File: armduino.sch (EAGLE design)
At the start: 64 parts, among them IC1 7805DT, IC2 LM358D, IC3 LM1117-3.3V, Q1 FDN360P, Q2 5MHz, Q3 8MHz, U1 MKL26Z128VFM4, U2 MKE02Z64VLD4, X1 POWERSUPPLY_DC21MMX, X2 USB-B_TH

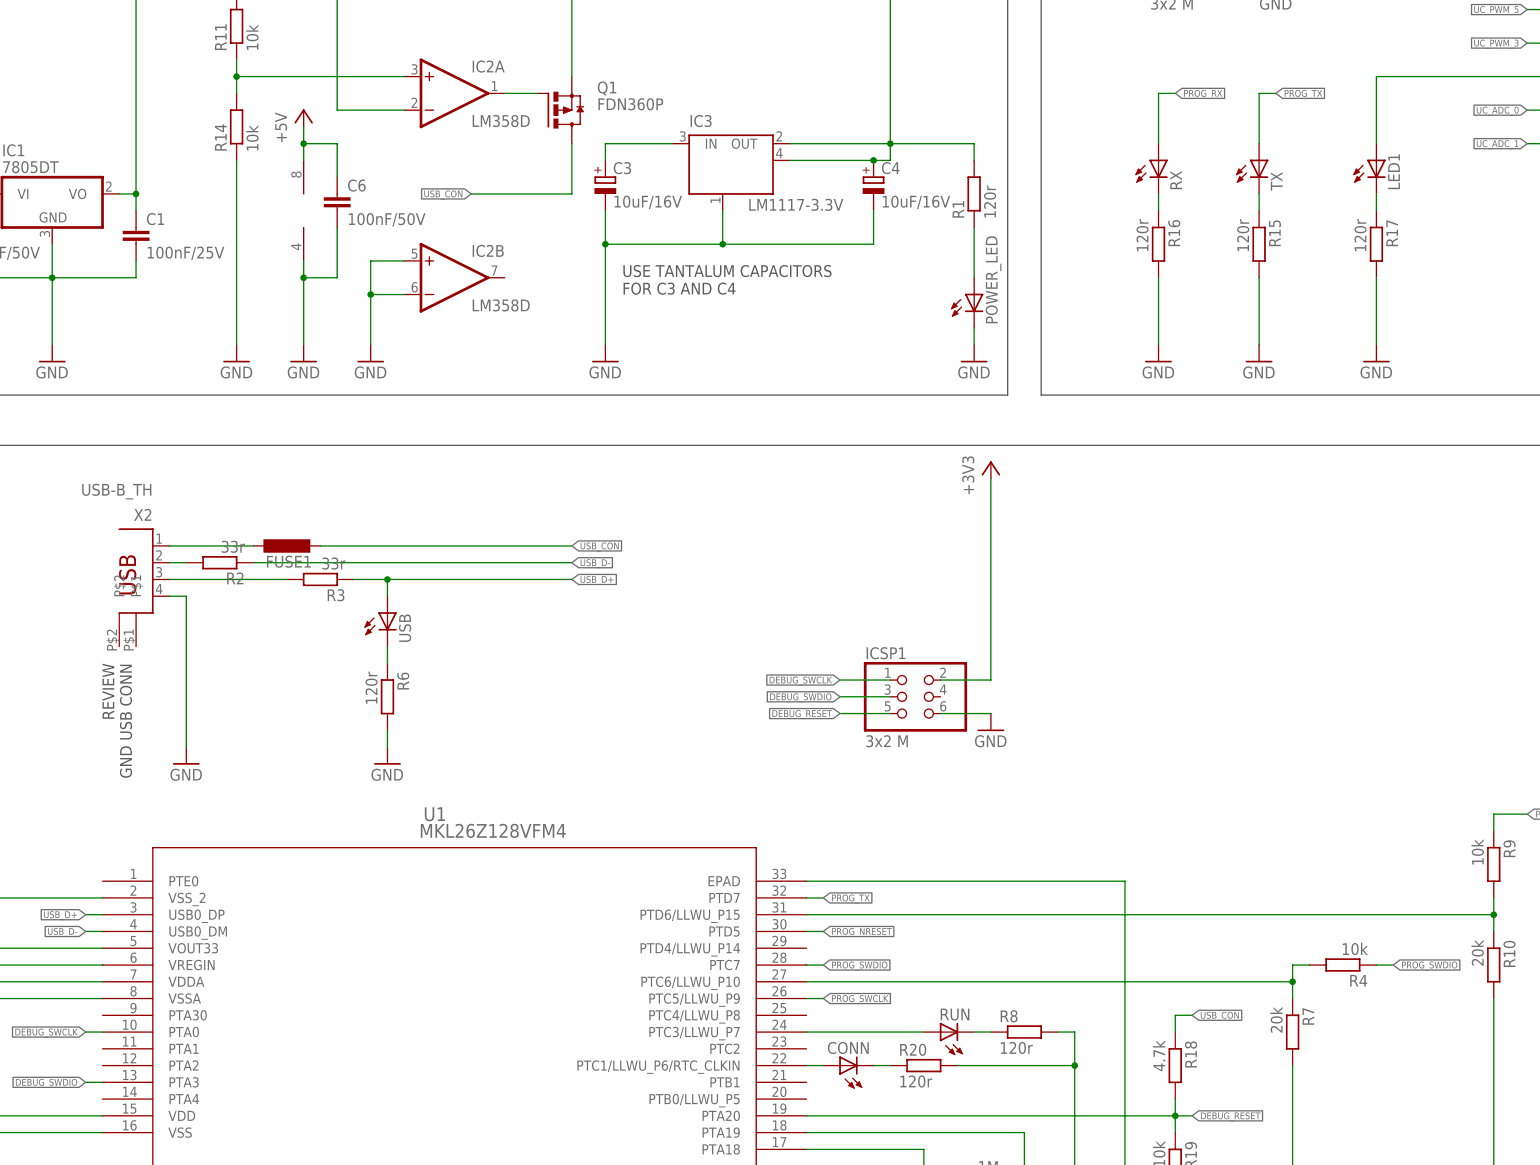
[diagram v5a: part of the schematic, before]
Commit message: Fixed target XTAL value, heat dissipation mask, update to version 0.7
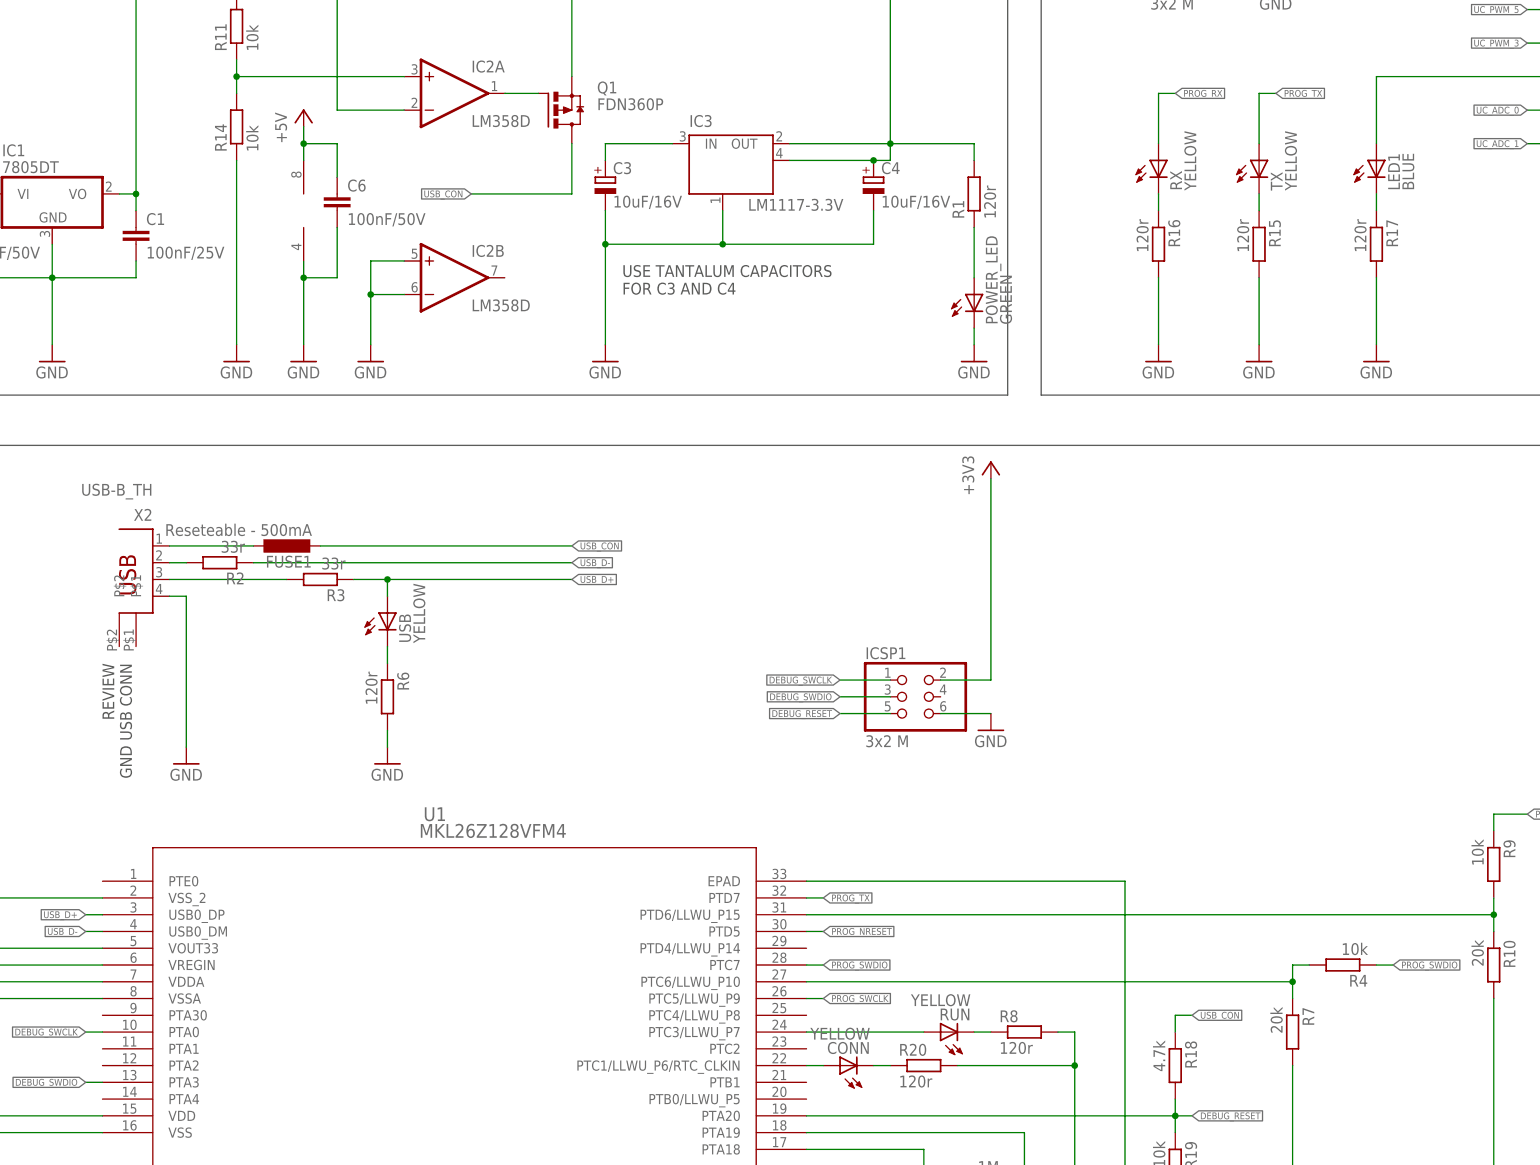
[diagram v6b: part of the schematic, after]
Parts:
- CONN, RUN, RX, TX, USB: value (none) -> YELLOW
- FUSE1: value (none) -> Reseteable - 500mA
- LED1: value (none) -> BLUE
- POWER_LED: value (none) -> GREEN
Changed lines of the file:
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@@
 <setting verticaltext="up"/>
 </settings>
-<grid distance="0.1" unitdist="inch" unit="inch" style="lines" multiple="1" display="yes" altdistance="0.01" altunitdist="inch" altunit="inch"/>
+<grid distance="0.1" unitdist="inch" unit="inch" style="lines" multiple="1" display="no" altdistance="0.01" altunitdist="inch" altunit="inch"/>
 <layers>
 <layer number="1" name="Top" color="4" fill="1" visible="no" active="no"/>
@@
 <part name="GND3" library="supply1" deviceset="GND" device=""/>
 <part name="D1" library="diode" deviceset="DIODE-" device="DO-214AC" value="1n4007"/>
-<part name="POWER_LED" library="led" deviceset="LED" device="CHIP-LED0805"/>
+<part name="POWER_LED" library="led" deviceset="LED" device="CHIP-LED0805" value="GREEN"/>
 <part name="R1" library="rcl" deviceset="R-EU_" device="M0805" value="120r"/>
 <part name="GND4" library="supply1" deviceset="GND" device=""/>
-<part name="FUSE1" library="rcl" deviceset="L-EU" device="L1812"/>
+<part name="FUSE1" library="rcl" deviceset="L-EU" device="L1812" value="Reseteable - 500mA"/>
 <part name="GND5" library="supply1" deviceset="GND" device=""/>
 <part name="R2" library="rcl" deviceset="R-EU_" device="M0805" value="33r"/>
 <part name="R3" library="rcl" deviceset="R-EU_" device="M0805" value="33r"/>
-<part name="USB" library="led" deviceset="LED" device="CHIP-LED0805"/>
+<part name="USB" library="led" deviceset="LED" device="CHIP-LED0805" value="YELLOW"/>
 <part name="R6" library="rcl" deviceset="R-EU_" device="M0805" value="120r"/>
 <part name="GND12" library="supply1" deviceset="GND" device=""/>
@@
 <part name="C17" library="rcl" deviceset="C-EU" device="C0805K" value="1uF/25V"/>
 <part name="GND22" library="supply1" deviceset="GND" device=""/>
-<part name="TX" library="led" deviceset="LED" device="CHIP-LED0805"/>
+<part name="TX" library="led" deviceset="LED" device="CHIP-LED0805" value="YELLOW"/>
 <part name="R15" library="rcl" deviceset="R-EU_" device="M0805" value="120r"/>
-<part name="RX" library="led" deviceset="LED" device="CHIP-LED0805"/>
+<part name="RX" library="led" deviceset="LED" device="CHIP-LED0805" value="YELLOW"/>
 <part name="R16" library="rcl" deviceset="R-EU_" device="M0805" value="120r"/>
 <part name="GND25" library="supply1" deviceset="GND" device=""/>
 <part name="GND26" library="supply1" deviceset="GND" device=""/>
 <part name="GND27" library="supply1" deviceset="GND" device=""/>
-<part name="LED1" library="led" deviceset="LED" device="CHIP-LED0805"/>
+<part name="LED1" library="led" deviceset="LED" device="CHIP-LED0805" value="BLUE"/>
 <part name="R17" library="rcl" deviceset="R-EU_" device="M0805" value="120r"/>
 <part name="GND28" library="supply1" deviceset="GND" device=""/>
@@
 <part name="R7" library="rcl" deviceset="R-EU_" device="M0805" value="20k"/>
 <part name="GND35" library="supply1" deviceset="GND" device=""/>
-<part name="RUN" library="led" deviceset="LED" device="CHIP-LED0805"/>
-<part name="CONN" library="led" deviceset="LED" device="CHIP-LED0805"/>
+<part name="RUN" library="led" deviceset="LED" device="CHIP-LED0805" value="YELLOW"/>
+<part name="CONN" library="led" deviceset="LED" device="CHIP-LED0805" value="YELLOW"/>
 <part name="R8" library="rcl" deviceset="R-EU_" device="M0805" value="120r"/>
 <part name="R20" library="rcl" deviceset="R-EU_" device="M0805" value="120r"/>

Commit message: Fixed 100nF caps to same value.
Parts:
- C11, C15, C6: value 100nF/50V -> 100nF/25V
- C12: value 100nF/50v -> 100nF/25V
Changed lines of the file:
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@@
 <part name="C9" library="rcl" deviceset="C-EU" device="C0805K" value="1uF/25V"/>
 <part name="C10" library="rcl" deviceset="C-EU" device="C0805K" value="1uF/25V"/>
-<part name="C11" library="rcl" deviceset="C-EU" device="C0805K" value="100nF/50V"/>
-<part name="C12" library="rcl" deviceset="C-EU" device="C0805K" value="100nF/50v"/>
+<part name="C11" library="rcl" deviceset="C-EU" device="C0805K" value="100nF/25V"/>
+<part name="C12" library="rcl" deviceset="C-EU" device="C0805K" value="100nF/25V"/>
 <part name="GND14" library="supply1" deviceset="GND" device=""/>
 <part name="GND15" library="supply1" deviceset="GND" device=""/>
@@
 <part name="GND18" library="supply1" deviceset="GND" device=""/>
 <part name="GND19" library="supply1" deviceset="GND" device=""/>
-<part name="C15" library="rcl" deviceset="C-EU" device="C0805K" value="100nF/50V"/>
+<part name="C15" library="rcl" deviceset="C-EU" device="C0805K" value="100nF/25V"/>
 <part name="GND20" library="supply1" deviceset="GND" device=""/>
 <part name="P+8" library="supply1" deviceset="+5V" device=""/>
@@
 <part name="P+6" library="supply1" deviceset="+5V" device=""/>
 <part name="GND10" library="supply1" deviceset="GND" device=""/>
-<part name="C6" library="rcl" deviceset="C-EU" device="C0805K" value="100nF/50V"/>
+<part name="C6" library="rcl" deviceset="C-EU" device="C0805K" value="100nF/25V"/>
 <part name="GND11" library="supply1" deviceset="GND" device=""/>
 <part name="P+10" library="supply1" deviceset="+5V" device=""/>
